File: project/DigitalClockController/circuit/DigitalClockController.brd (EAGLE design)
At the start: 91.4 x 27.9 mm, 20 parts, among them IC2 PIC16F886, IC3 TBD62783APG, IC4 TBD62083APG, Q1 32.768kHz, Q2 20MHz

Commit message: ロゴを修正
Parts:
- moved IC2 53.3 mm to (35.6, 7.62)
- moved IC3 53.3 mm to (71.1, 14.0)
- moved IC4 53.3 mm to (11.4, 14.0)
- moved JP1 53.3 mm to (83.8, 22.9)
- moved JP2 53.3 mm to (83.8, 5.08)
- moved JP3 53.3 mm to (83.8, 14.0)
- moved Q1 53.3 mm to (22.9, 14.0)
- moved R1 53.3 mm to (54.6, 19.1)
- moved R2 53.3 mm to (44.5, 19.1)
- moved R3 53.3 mm to (34.3, 19.1)
- moved S1 53.3 mm to (59.7, 19.1)
- moved S2 53.3 mm to (49.5, 19.1)
- moved S3 53.3 mm to (39.4, 19.1)
- moved SV1 53.3 mm to (78.7, 14.0)
- moved SV2 53.3 mm to (3.81, 14.0)
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
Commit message: ガーバーデータを作成
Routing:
- net +5V: track 111.0 -> 110.2 mm, vias 1 -> 0
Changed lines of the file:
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@@
 <contactref element="S2" pad="3"/>
 <contactref element="JP2" pad="1"/>
-<wire x1="31.75" y1="3.81" x2="33.02" y2="2.54" width="1.016" layer="1"/>
-<wire x1="33.02" y1="2.54" x2="34.29" y2="1.27" width="1.016" layer="1"/>
+<wire x1="31.75" y1="3.81" x2="34.29" y2="1.27" width="1.016" layer="1"/>
 <wire x1="34.29" y1="1.27" x2="55.88" y2="1.27" width="1.016" layer="1"/>
 <wire x1="86.36" y1="10.16" x2="83.82" y2="7.62" width="1.016" layer="1"/>
 <wire x1="86.36" y1="10.16" x2="87.63" y2="10.16" width="1.016" layer="1"/>
 <wire x1="55.88" y1="1.27" x2="80.01" y2="1.27" width="1.016" layer="1"/>
-<via x="33.02" y="2.54" extent="1-16" drill="0.35"/>
 <wire x1="46.859075" y1="17.5514" x2="47.679725" y2="17.5514" width="0.1524" layer="16"/>
 <wire x1="41.6306" y1="15.7988" x2="45.106475" y2="15.7988" width="0.1524" layer="16"/>
@@
 <wire x1="55.266475" y1="15.7988" x2="57.019075" y2="17.5514" width="0.1524" layer="16"/>
 <wire x1="57.839725" y1="17.5514" x2="59.592325" y2="15.7988" width="0.1524" layer="16"/>
-<wire x1="33.02" y1="2.54" x2="33.02" y2="5.08" width="0.1524" layer="16"/>
-<wire x1="33.02" y1="5.08" x2="37.8206" y2="9.8806" width="0.1524" layer="16"/>
 <wire x1="49.432325" y1="13.2499625" x2="49.432325" y2="15.7988" width="0.1524" layer="16"/>
 <wire x1="48.641" y1="12.4586375" x2="49.432325" y2="13.2499625" width="0.1524" layer="16"/>
 <wire x1="47.3582375" y1="9.8806" x2="48.641" y2="11.1633625" width="0.1524" layer="16"/>
 <wire x1="48.641" y1="11.1633625" x2="48.641" y2="12.4586375" width="0.1524" layer="16"/>
-<wire x1="37.8206" y1="9.8806" x2="47.3582375" y2="9.8806" width="0.1524" layer="16"/>
+<wire x1="47.3582375" y1="9.8806" x2="37.8206" y2="9.8806" width="0.1524" layer="16"/>
 <wire x1="83.82" y1="7.62" x2="83.82" y2="5.08" width="1.016" layer="1"/>
 <wire x1="80.01" y1="1.27" x2="83.82" y2="5.08" width="1.016" layer="1"/>
+<wire x1="37.8206" y1="9.8806" x2="31.75" y2="3.81" width="0.1524" layer="16"/>
 </signal>
 <signal name="N$3">

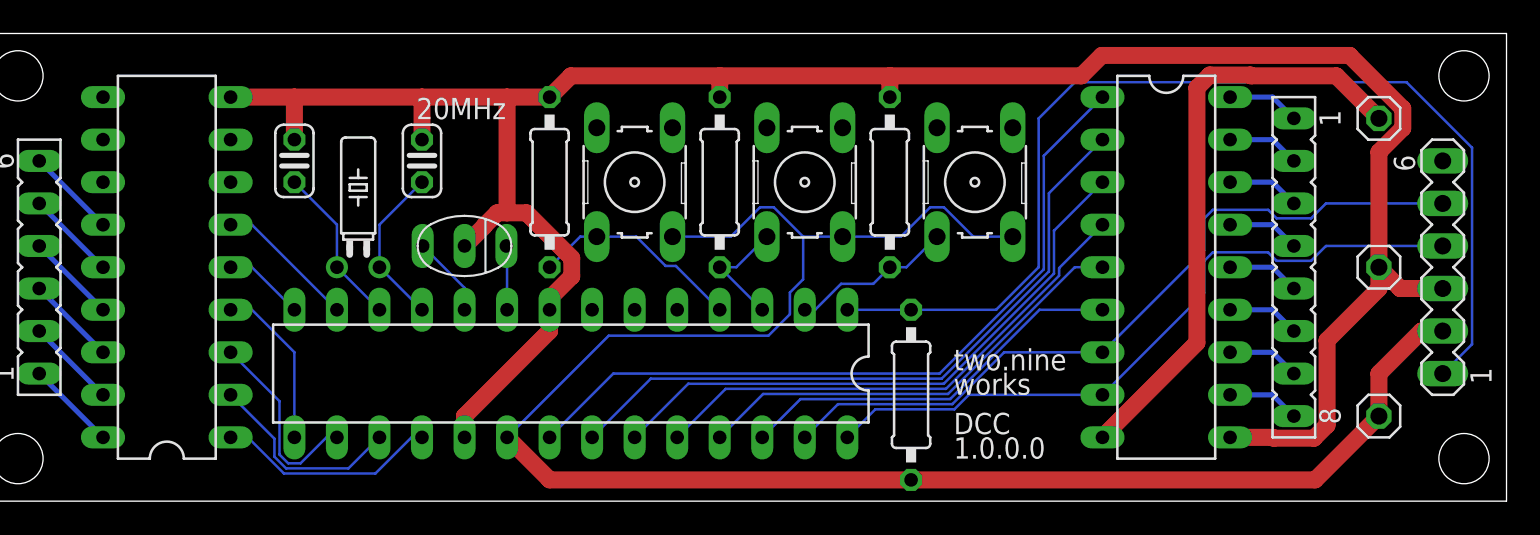
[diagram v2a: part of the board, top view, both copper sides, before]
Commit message: レイアウトに自由度が出るようにDisplay接続端子を増やす
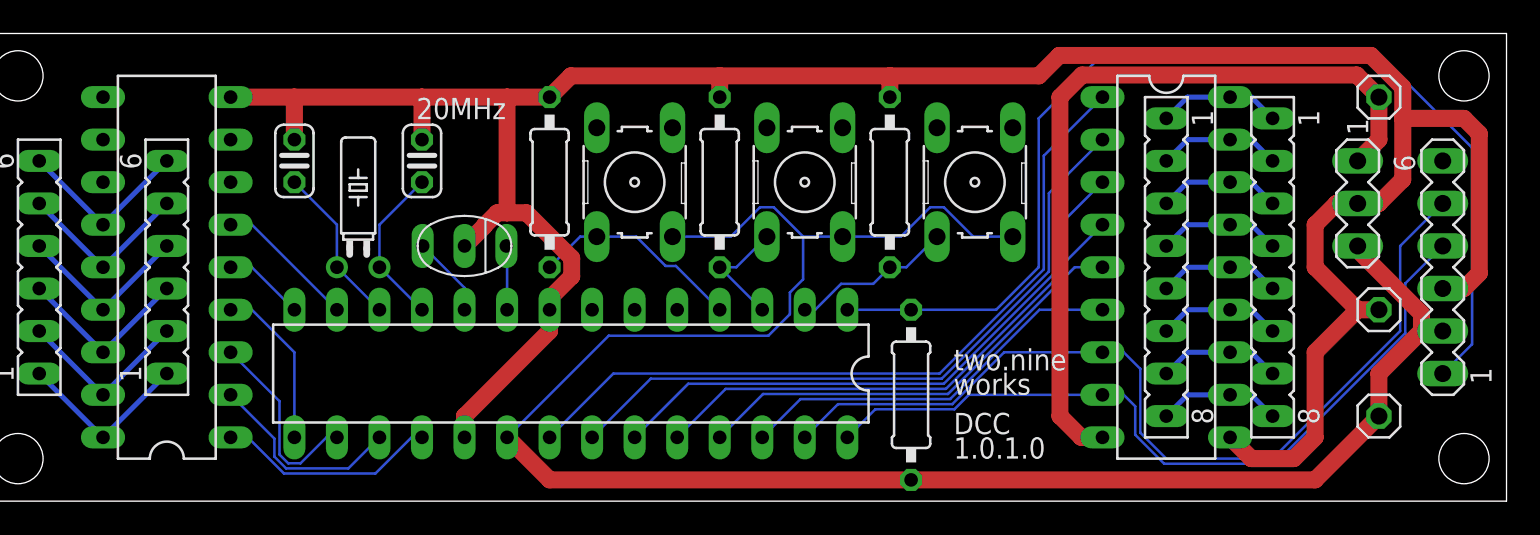
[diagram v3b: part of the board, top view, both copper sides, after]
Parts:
- added SV4: Digit, con-lsta:FE06
- added SV5: PICKit3, con-lstb:MA06-1
- added SV6: (no value), con-lstb:MA03-1
- SV2: value Digit -> Segment; device con-lsta:FE06 -> con-lsta:FE08
- SV3: value PICKit3 -> Digit; device con-lstb:MA06-1 -> con-lsta:FE06
- moved SV3 83.8 mm to (3.81, 14.0)
- moved SV2 67.3 mm to (71.1, 14.0), turned to 270 degrees
- moved JP3 2.54 mm to (83.8, 11.4)
- moved JP1 1.27 mm to (83.8, 24.1)
- moved SV1 1.27 mm to (77.5, 14.0)
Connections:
- net +12V: now also SV6.1
- net +5V: now also SV5.2, SV6.3; no longer SV3.2
- net GND: now also SV5.3, SV6.2; no longer SV3.3
- net N$10: now also SV2.2
- net N$11: now also SV2.3
- net N$12: now also SV2.4
- net N$14: now also SV5.5; no longer SV3.5
- net N$27: now also SV2.5
- net N$28: now also SV2.6
- net N$29: now also SV2.7
- net N$30: now also SV2.8
- net N$31: now also SV3.1, SV4.1; no longer SV2.1
- net N$32: now also SV3.2, SV4.2; no longer SV2.2
- net N$33: now also SV3.3, SV4.3; no longer SV2.3
- net N$34: now also SV3.4, SV4.4; no longer SV2.4
- net N$35: now also SV3.5, SV4.5; no longer SV2.5
- net N$36: now also SV3.6, SV4.6; no longer SV2.6
- net N$37: now also SV5.4; no longer SV3.4
- net N$8: now also SV5.1; no longer SV3.1
- net N$9: now also SV2.1
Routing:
- net GND: track 139.8 -> 158.0 mm
- net +12V: track 35.5 -> 46.6 mm
- net N$14: track 45.4 -> 54.4 mm
- net +5V: track 110.2 -> 116.9 mm
- net N$35: track 5.39 -> 10.8 mm
- net N$34: track 5.39 -> 10.8 mm
- net N$32: track 5.39 -> 10.8 mm
- net N$36: track 5.39 -> 10.8 mm
- net N$33: track 5.39 -> 10.8 mm
- net N$31: track 5.39 -> 10.8 mm
- net N$37: track 41.8 -> 46.4 mm
- net N$27: track 4.34 -> 7.40 mm
- net N$12: track 4.34 -> 7.40 mm
- net N$29: track 4.34 -> 7.40 mm
- net N$9: track 4.34 -> 7.40 mm
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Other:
- board text added: "DCC 1.0.1.0"
- board text removed: "DCC 1.0.0.0"

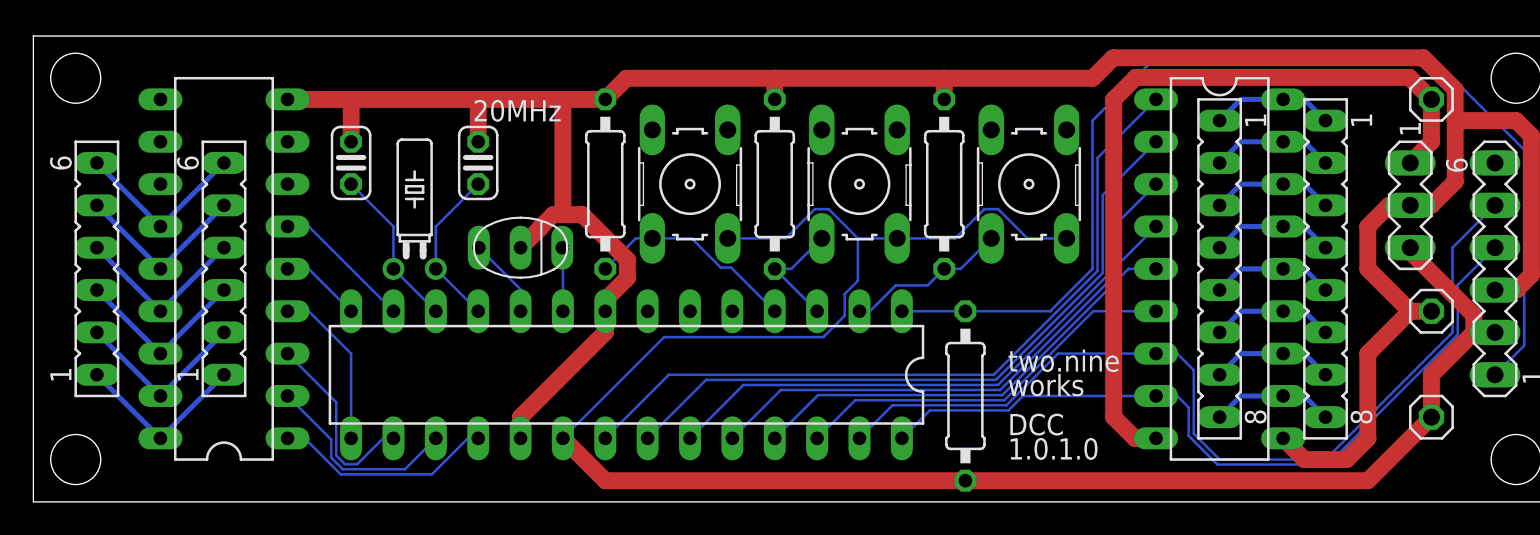
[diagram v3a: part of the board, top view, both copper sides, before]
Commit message: ピン配置修正、5V-12V共通ジャンパ追加
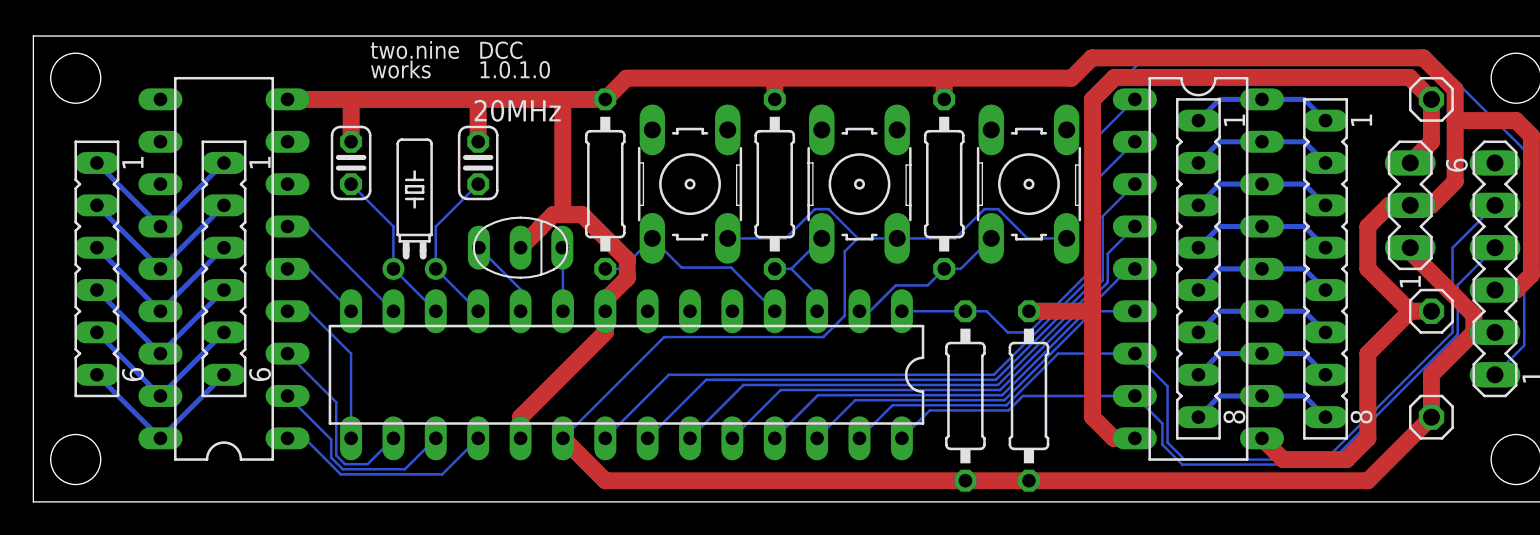
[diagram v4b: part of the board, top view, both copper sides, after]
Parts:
- added R5: 0, rcl:0207/10
- moved IC3 1.27 mm to (69.8, 14.0)
- moved SV2 1.27 mm to (69.8, 14.0)
- turned SV3 to 270 degrees
- turned SV4 to 270 degrees
- turned SV6 to 90 degrees
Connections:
- net +12V: now also R5.1, SV6.3; no longer SV6.1
- net +5V: now also R5.2, SV6.1; no longer SV6.3
- net N$31: now also IC4.13; no longer IC4.18
- net N$32: now also IC4.14; no longer IC4.17
- net N$33: now also IC4.15; no longer IC4.16
- net N$34: now also IC4.16; no longer IC4.15
- net N$35: now also IC4.17; no longer IC4.14
- net N$36: now also IC4.18; no longer IC4.13
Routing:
- net +12V: track 46.6 -> 51.7 mm
- net N$8: track 65.0 -> 66.5 mm
- net N$9: track 7.40 -> 8.67 mm
- net N$30: track 7.40 -> 8.67 mm
- net N$28: track 7.40 -> 8.67 mm
- net N$11: track 7.40 -> 8.67 mm
- net N$10: track 7.40 -> 8.67 mm
- net N$29: track 7.40 -> 8.67 mm
- net N$27: track 7.40 -> 8.67 mm
- net N$12: track 7.40 -> 8.67 mm
- net N$13: track 23.5 -> 22.2 mm
- net N$15: track 27.1 -> 25.8 mm
- net GND: track 158.0 -> 159.3 mm
- net N$23: track 35.8 -> 35.2 mm
- net N$22: track 30.9 -> 30.4 mm
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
